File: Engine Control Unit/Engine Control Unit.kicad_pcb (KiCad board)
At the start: 2 copper layers, 33 x 57 mm, 9 parts, among them J3 Conn_01x02_Socket

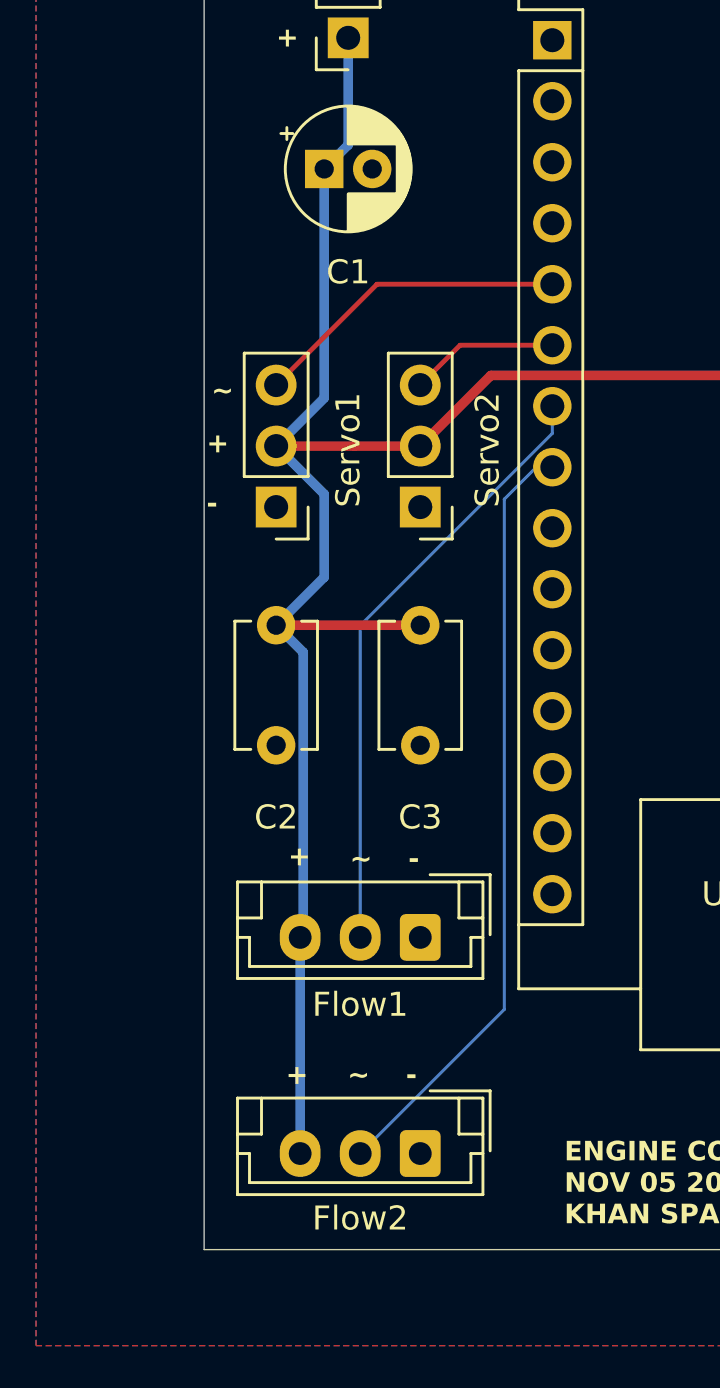
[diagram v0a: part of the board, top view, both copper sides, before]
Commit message: :sparkles: (Ground Control) Started new ground control suite, arduino code ready for testing
Now outputs a csv of data and expects constant serial communication about valve position, defaults to emergency closed
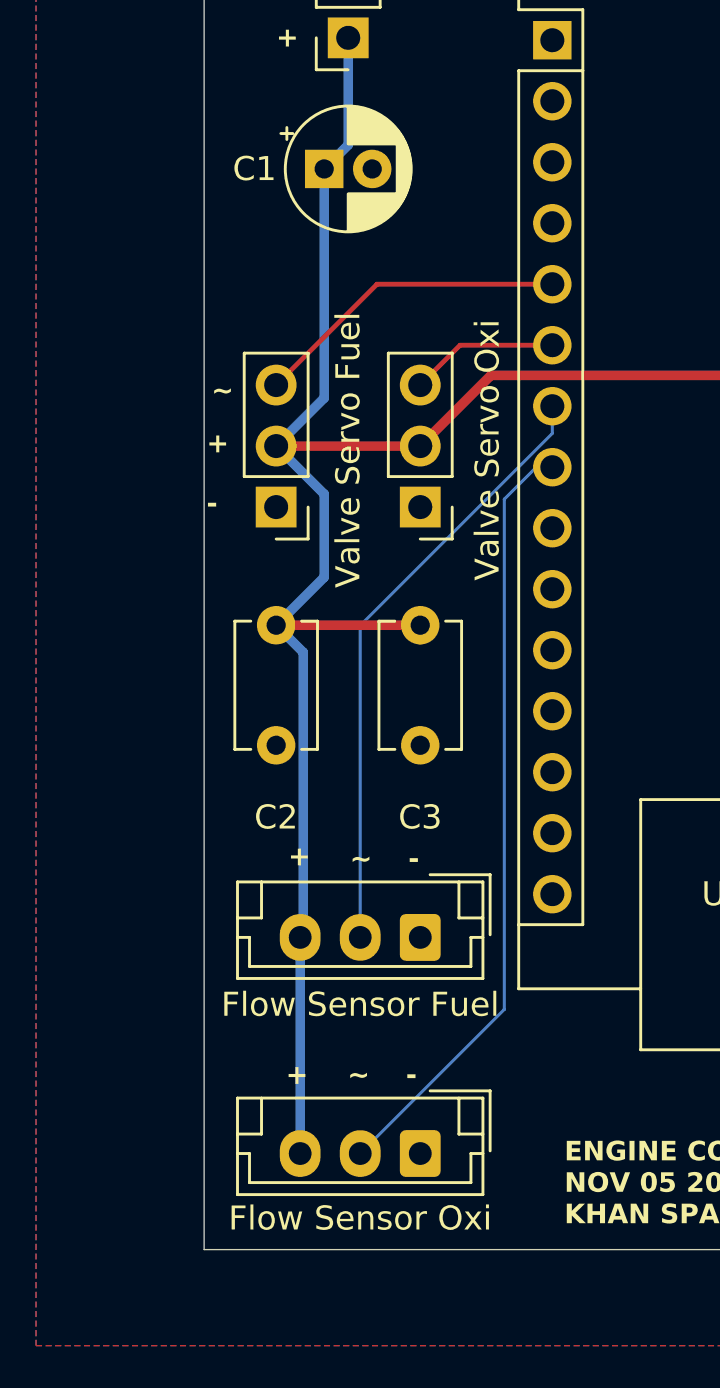
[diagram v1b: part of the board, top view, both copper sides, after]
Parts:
- Flow Sensor Fuel: renamed from Flow1
- Flow Sensor Oxi: renamed from Flow2
- Valve Servo Fuel: renamed from Servo1
- Valve Servo Oxi: renamed from Servo2
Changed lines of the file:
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@@
 		(descr "Through hole straight pin header, 1x03, 2.54mm pitch, single row")
 		(tags "Through hole pin header THT 1x03 2.54mm single row")
-		(property "Reference" "Servo1"
+		(property "Reference" "Valve Servo Fuel"
 			(at -3 2.38 90)
 			(layer "F.SilkS")
@@
 		(tags "CP Radial series Radial pin pitch 2.00mm  diameter 5mm Electrolytic Capacitor")
 		(property "Reference" "C1"
-			(at 1 4.3 0)
+			(at -2.9 0 0)
 			(layer "F.SilkS")
 			(effects
@@
 		(descr "JST EH series connector, B3B-EH-A (http://www.jst-mfg.com/product/pdf/eng/eEH.pdf), generated with kicad-footprint-generator")
 		(tags "connector JST EH vertical")
-		(property "Reference" "Flow1"
+		(property "Reference" "Flow Sensor Fuel"
 			(at 2.5 -2.8 0)
 			(layer "F.SilkS")
@@
 		(descr "Through hole straight pin header, 1x03, 2.54mm pitch, single row")
 		(tags "Through hole pin header THT 1x03 2.54mm single row")
-		(property "Reference" "Servo2"
+		(property "Reference" "Valve Servo Oxi"
 			(at -2.8 2.38 90)
 			(layer "F.SilkS")
@@
 		(descr "JST EH series connector, B3B-EH-A (http://www.jst-mfg.com/product/pdf/eng/eEH.pdf), generated with kicad-footprint-generator")
 		(tags "connector JST EH vertical")
-		(property "Reference" "Flow2"
+		(property "Reference" "Flow Sensor Oxi"
 			(at 2.5 -2.7 0)
 			(layer "F.SilkS")

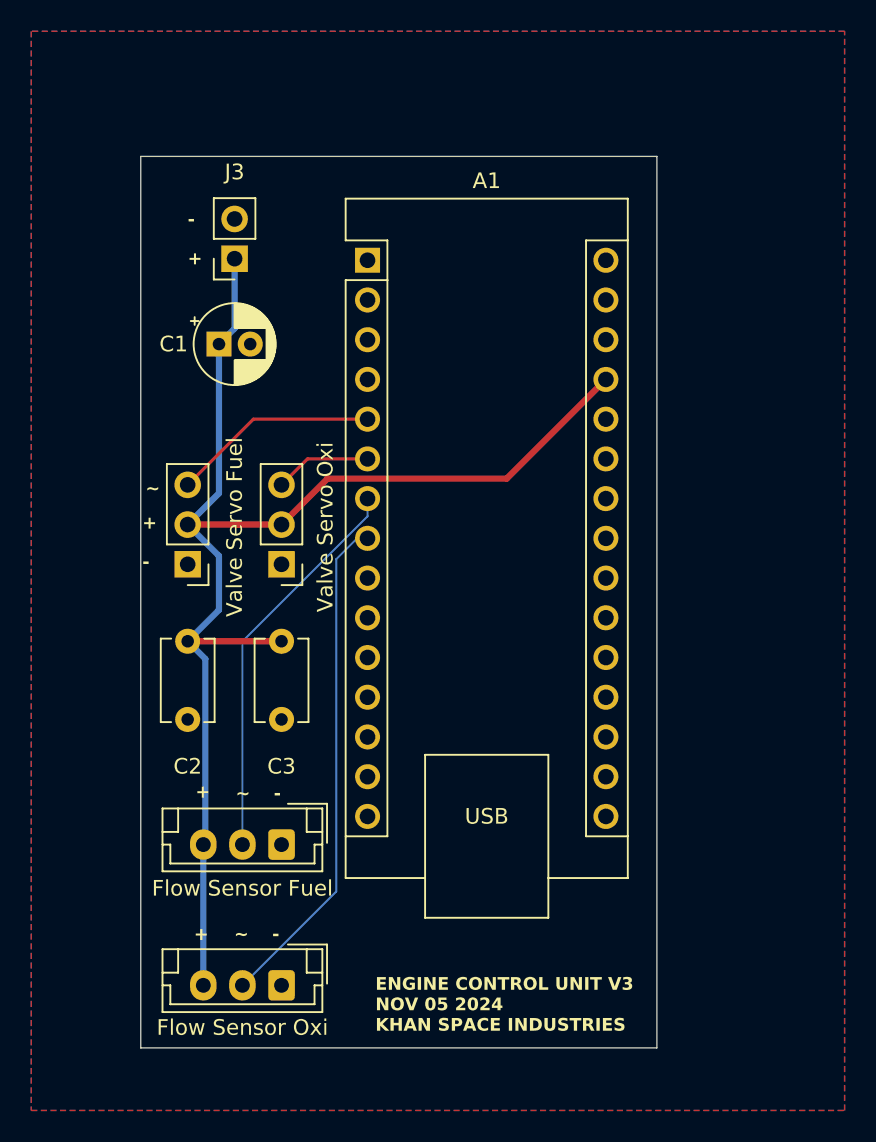
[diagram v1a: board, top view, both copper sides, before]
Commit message: :bug: (Pins) Change pins to interupt
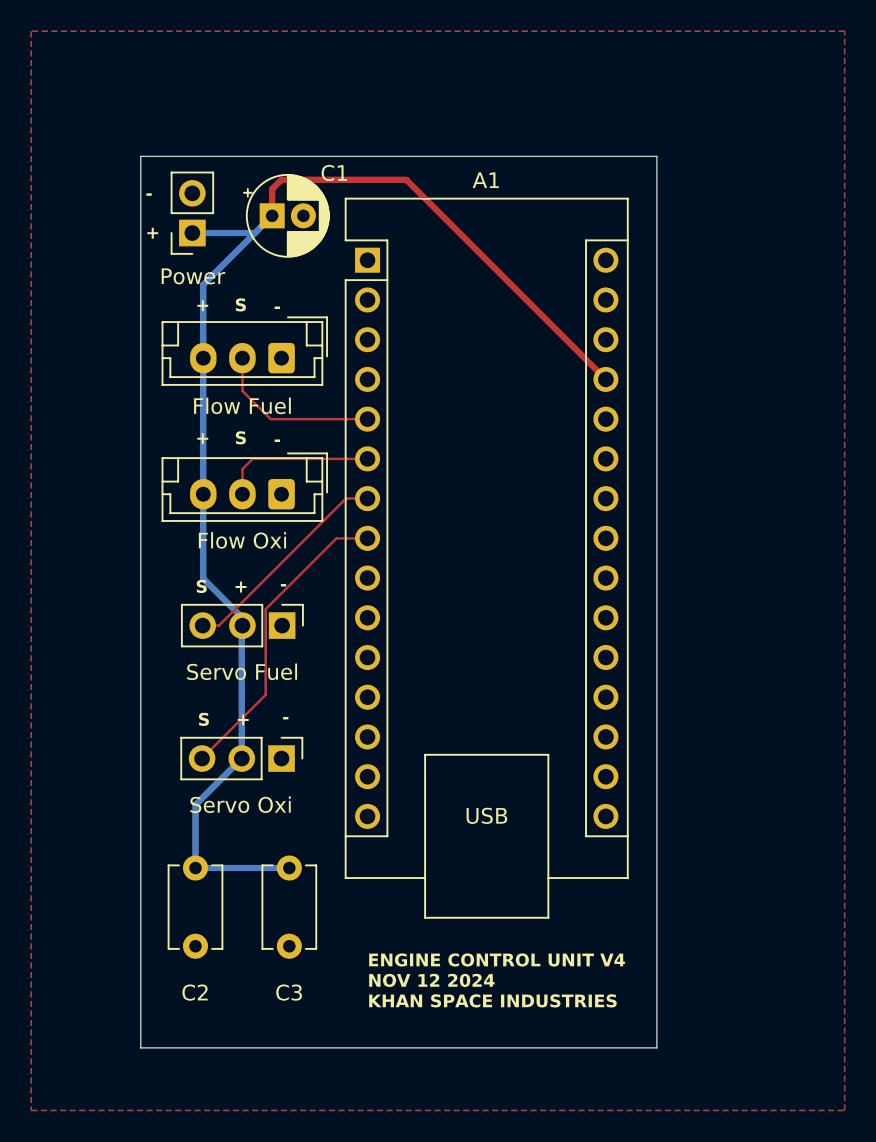
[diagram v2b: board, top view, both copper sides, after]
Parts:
- Flow Fuel: renamed from Flow Sensor Fuel
- Flow Oxi: renamed from Flow Sensor Oxi
- Servo Fuel: renamed from Valve Servo Fuel
- Servo Oxi: renamed from Valve Servo Oxi
- moved Flow Oxi 31.4 mm to (135.0, 96.6)
- moved Flow Fuel 31.1 mm to (135.0, 87.9)
- moved C2 14.5 mm to (129.5, 125.5)
- moved C3 14.5 mm to (135.5, 125.5)
- moved Servo Oxi 12.4 mm to (135.0, 113.5), turned to -90 degrees
- moved C1 8.88 mm to (134.4, 78.8)
- moved Servo Fuel 7.20 mm to (135.0, 105.0), turned to -90 degrees
- moved Power 3.16 mm to (129.3, 79.9)
- renumbered J3 to Power
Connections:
- Flow Fuel pad 2: Net-(A1-D4) -> Net-(A1-D2)
- Flow Oxi pad 2: Net-(A1-D5) -> Net-(A1-D3)
- Servo Fuel pad 3: Net-(A1-D2) -> Net-(A1-D4)
- Servo Oxi pad 3: Net-(A1-D3) -> Net-(A1-D5)
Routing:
- net Net-(A1-D5): track 32.3 -> 20.3 mm
- net Net-(A1-D4): track 25.4 -> 13.9 mm
- net Net-(A1-D3): track 6.19 -> 9.87 mm
- net Net-(A1-D2): track 13.2 -> 10.8 mm
- net +5V: track 87.2 -> 85.9 mm
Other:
- board text added: "ENGINE CONTROL UNIT V4 NOV 12 2024 KHAN SPACE INDUSTRIES"
- board text added: "S"
- board text removed: "ENGINE CONTROL UNIT V3 NOV 05 2024 KHAN SPACE INDUSTRIES"
- board text removed: "~"
